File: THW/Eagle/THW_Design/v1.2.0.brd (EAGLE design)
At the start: 100 x 200 mm, 41 parts, among them U1 ADA4091-2ARZ-RL

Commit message: commit
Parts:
- removed C1: 0805YC103J4T2A, 0805YC103J4T2A:CAPC2012X94N
- removed R1, R2, R3: (no value), resistor:M0805
- removed U1: ADA4091-2ARZ-RL, ADA4091-2ARZ-RL:SOIC127P600X175-8N
- moved POWER 20.0 mm to (58.2, 199.9)
- moved TP3 20.0 mm to (40.1, 198.0)
- moved WB_SENS2 20.0 mm to (78.0, 199.9)
- moved TP1 19.8 mm to (54.1, 174.7)
- moved TP25 17.1 mm to (29.8, 163.8)
- moved R7 8.74 mm to (49.5, 173.4), turned to 180 degrees
- moved TP27 8.60 mm to (36.3, 166.7)
- moved R4 6.00 mm to (45.4, 173.4), turned to 180 degrees
- moved R_CURRENT 5.59 mm to (40.5, 174.7), turned to 270 degrees
- moved TP28 2.58 mm to (34.4, 163.8)
- moved TP26 1.42 mm to (31.7, 166.8)
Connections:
- removed net GND: C1.2, POWER.6, R3.2, U1.3, U1.4, WB_SENS2.8
- removed net LONG_HW+: U1.2
- removed net LONG_HW_SENS-: LONG_HW-.P$1, TP28.TP, WB_SENS1.2
- removed net N$2: R1.1, U1.5
- removed net N$4: R2.2, R3.1, U1.6
- removed net OPAMP_OUTPUT: R2.1, U1.7, WB_SENS2.7
- removed net SHORT_HW_SENS+: SHORT_HW+.P$2, TP26.TP, WB_SENS1.8
- removed net SHORT_HW_SENS-: LONG_HW+.P$2, SHORT_HW-.P$1, TP25.TP, TP27.TP, WB_SENS1.1, WB_SENS1.5, WB_SENS1.7
- removed net SUMMING_OP_AMP: R1.2, R4.1, R7.2, WB_SENS1.6, WB_SENS2.4, WB_SENS2.5
- removed net VSS: C1.1, POWER.5, U1.8
- new net NODE_B: R4.1, R7.2, WB_SENS1.7, WB_SENS2.4, WB_SENS2.6
- net SHORT_HW+: now also SHORT_HW+.P$2, TP26.TP, WB_SENS1.2, WB_SENS2.5, WB_SENS2.8; no longer WB_SENS2.2, WB_SENS2.3
- net SHORT_HW-: now also LONG_HW+.P$2, SHORT_HW-.P$1, TP25.TP, TP27.TP, WB_SENS1.1, WB_SENS1.6, WB_SENS1.8
- net WB_CURRENT+: now also POWER.2, WB_SENS2.7; no longer POWER.3, WB_SENS2.1
- net WB_CURRENT-: now also LONG_HW-.P$1, POWER.1, TP28.TP, WB_SENS1.5, WB_SENS2.3; no longer POWER.4, U1.1, WB_SENS2.6
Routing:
- net SHORT_HW-: track 14.8 -> 619.0 mm, vias 2 -> 7
- net SHORT_HW_SENS-: track 326.8 -> 0.00 mm, vias 2 -> 0
- net SHORT_HW+: track 59.5 -> 219.9 mm, vias 3 -> 5
- net WB_CURRENT-: track 65.3 -> 177.7 mm, vias 3 -> 4
- net NODE_B: track 0.00 -> 81.0 mm, vias 0 -> 3
- net PT_CURRENT-: track 212.6 -> 150.7 mm
- net WB_CURRENT+: track 28.5 -> 60.9 mm
- net PT_CURRENT+: track 330.4 -> 306.7 mm
- net PT3_S-: track 88.0 -> 82.6 mm
- net PT3_S+: track 84.5 -> 80.4 mm
- net SUMMING_OP_AMP: track 2.96 -> 0.00 mm, vias 2 -> 0
- net PT4_S+: track 213.8 -> 212.7 mm
- net PT0_S+: track 90.8 -> 89.8 mm
- net PT2_S-: track 132.3 -> 133.1 mm
- net PT2_S+: track 134.6 -> 134.0 mm
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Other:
- board text removed: "Wheatstone bridge"

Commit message: new traces
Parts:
- removed PT$0: PTS1206A, PTS1206:CAPMP3216X166
- removed R4, R7: (no value), resistor:M0805
- removed TP1, TP10, TP12, TP14, TP16, TP18, TP2, TP20, TP22, TP24, TP25, TP26, TP27, TP28, TP3, TP4, TP6, TP8: TPTP10SQ, testpad:TP10SQ
- added POT_1, POT_2, POT_LONG_HW, POT_SHORT_HW: 67WR200LFR$1, POTENTIOMETER_67WR200LFR:67WR200LF
- added PT$6: PTS1206A, PTS1206:CAPMP3216X166
- moved PT$1 89.4 mm to (50.0, 126.2), turned to 0 degrees
- moved PT$3 72.9 mm to (73.6, 61.1), flipped to the bottom, turned to 90 degrees
- moved PT$5 42.0 mm to (26.4, 40.1), turned to 90 degrees
- moved PT$2 42.0 mm to (73.6, 103.1), flipped to the top
- moved R_CURRENT 4.47 mm to (36.5, 172.7)
- moved PT$4 3.93 mm to (50.0, 16.8), turned to 180 degrees
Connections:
- removed net PT0_S+: PT$0.SENS+, PT_SENS2.3, TP2.TP
- removed net PT0_S-: PT$0.SENS-, PT_SENS2.4, TP4.TP
- removed net PT1_S+: PT$1.SENS+, PT_SENS1.2, TP10.TP
- removed net PT1_S-: PT$1.SENS-, PT_SENS1.1, TP12.TP
- removed net PT2_S+: PT$2.SENS+, PT_SENS2.5, TP6.TP
- removed net PT2_S-: PT$2.SENS-, PT_SENS2.6, TP8.TP
- removed net PT3_S+: PT$3.SENS+, PT_SENS2.2, TP18.TP
- removed net PT3_S-: PT$3.SENS-, PT_SENS2.1, TP20.TP
- removed net PT4_S+: PT$4.SENS+, PT_SENS2.8, TP14.TP
- removed net PT4_S-: PT$4.SENS-, PT_SENS2.7, TP16.TP
- removed net PT5_S+: PT$5.SENS+, PT_SENS1.4, TP22.TP
- removed net PT5_S-: PT$5.SENS-, PT_SENS1.3, TP24.TP
- new net N$1: LONG_HW-.P$1, LONG_HW-.P$2, POT_LONG_HW.P$2
- new net N$2: PT$1.-, PT$2.+, PT_SENS2.2, PT_SENS2.3
- new net N$3: PT$2.-, PT$3.+, PT_SENS2.4, PT_SENS2.5
- new net N$4: PT$3.-, PT$4.+, PT_SENS2.6, PT_SENS2.7
- new net N$5: PT$4.-, PT$5.+, PT_SENS1.1, PT_SENS2.8
- new net N$6: PT$5.-, PT$6.+, PT_SENS1.2, PT_SENS1.3
- new net N$8: POT_SHORT_HW.P$1, SHORT_HW+.P$1, SHORT_HW+.P$2
- net NODE_B: now also POT_1.P$1, POT_2.P$2, WB_SENS1.1; no longer R4.1, R7.2, WB_SENS1.7
- net PT_CURRENT+: now also PT_SENS2.1; no longer PT$0.+, PT$0.-, PT$1.-, PT$2.+, PT$2.-, PT$3.+, PT$3.-, PT$4.+, PT$4.-, PT$5.+, TP1.TP
- net PT_CURRENT-: now also PT$6.-, PT_SENS1.4; no longer PT$5.-, TP3.TP
- net SHORT_HW+: now also POT_1.P$2, POT_SHORT_HW.P$2; no longer R4.2, SHORT_HW+.P$1, SHORT_HW+.P$2, TP26.TP, WB_SENS1.2
- net SHORT_HW-: now also WB_SENS1.2; no longer TP25.TP, TP27.TP, WB_SENS1.1, WB_SENS1.6, WB_SENS1.8
- net WB_CURRENT-: now also POT_2.P$1, POT_LONG_HW.P$1, POWER.5; no longer LONG_HW-.P$1, LONG_HW-.P$2, POWER.1, R7.1, TP28.TP, WB_SENS1.5
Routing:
- net SHORT_HW-: track 619.0 -> 237.7 mm, vias 7 -> 4
- net PT_CURRENT+: track 306.7 -> 0.00 mm, vias 12 -> 0
- net PT4_S+: track 212.7 -> 0.00 mm, vias 2 -> 0
- net PT4_S-: track 206.2 -> 0.00 mm, vias 2 -> 0
- net SHORT_HW+: track 219.9 -> 20.7 mm, vias 5 -> 3
- net PT1_S+: track 159.7 -> 0.00 mm, vias 2 -> 0
- net PT1_S-: track 153.9 -> 0.00 mm, vias 2 -> 0
- net WB_CURRENT-: track 177.7 -> 25.9 mm, vias 4 -> 2
- net PT_CURRENT-: track 150.7 -> 0.00 mm, vias 2 -> 0
- net PT2_S+: track 134.0 -> 0.00 mm, vias 2 -> 0
- net PT2_S-: track 133.1 -> 0.00 mm, vias 2 -> 0
- net PT5_S+: track 114.2 -> 0.00 mm, vias 2 -> 0
- net PT5_S-: track 108.6 -> 0.00 mm, vias 2 -> 0
- net PT0_S+: track 89.8 -> 0.00 mm, vias 2 -> 0
- net PT0_S-: track 88.3 -> 0.00 mm, vias 2 -> 0
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
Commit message: Some polygon work for Asad
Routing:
- net WB_CURRENT-: track 25.9 -> 2.88 mm
- net SHORT_HW+: track 20.7 -> 2.02 mm
- net NODE_B: track 30.6 -> 22.1 mm
- net N$1: track 35.0 -> 28.7 mm
- net N$8: track 33.4 -> 29.3 mm
- added copper zone on layer 2, net N$1
- added copper zone on layer 2, net N$8
- added copper zone on layer 2, net NODE_B
- added copper zone on layer 2, net SHORT_HW+
- added copper zone on layer 2, net WB_CURRENT-
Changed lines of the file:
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@@
 <via x="52.21" y="170.34" extent="1-16" drill="0.35"/>
 <via x="46.88" y="172.8" extent="1-16" drill="0.35"/>
-<wire x1="50.81" y1="172.49" x2="49.4" y2="173.9" width="6.5" layer="2"/>
-<wire x1="49.4" y1="173.9" x2="49.30791875" y2="173.9" width="6.5" layer="2"/>
-<wire x1="49.4" y1="173.9" x2="44.9" y2="178.4" width="6.5" layer="2"/>
 <wire x1="29.4738" y1="178.4" x2="44.9" y2="178.4" width="6.5" layer="2"/>
 <contactref element="WB_SENS1" pad="1"/>
@@
 <wire x1="27.719" y1="182.588" x2="27.719" y2="180.1548" width="2" layer="2"/>
 <wire x1="27.719" y1="180.1548" x2="28.9869" y2="178.8869" width="2" layer="2"/>
+<polygon width="0.15" layer="2">
+<vertex x="53.9" y="169.4"/>
+<vertex x="49.1" y="169.4"/>
+<vertex x="43.5" y="175"/>
+<vertex x="43.5" y="181.4"/>
+<vertex x="43.6" y="181.5"/>
+<vertex x="48.4" y="181.5"/>
+<vertex x="49.2" y="180.7"/>
+<vertex x="49.2" y="178.4"/>
+<vertex x="53.9" y="173.7"/>
+</polygon>
 <wire x1="68.494" y1="184.65" x2="70.524" y2="184.65" width="0" layer="19" extent="1-1"/>
-<wire x1="50.81" y1="172.49" x2="68.494" y2="184.65" width="0" layer="19" extent="1-2"/>
-<wire x1="52.21" y1="170.34" x2="50.81" y2="172.49" width="0" layer="19" extent="1-2"/>
-<wire x1="46.88" y1="172.8" x2="49.30791875" y2="173.9" width="0" layer="19" extent="1-2"/>
+<wire x1="52.21" y1="170.34" x2="68.494" y2="184.65" width="0" layer="19" extent="1-1"/>
 </signal>
 <signal name="SHORT_HW+">
@@
 <contactref element="POT_SHORT_HW" pad="P$2"/>
 <contactref element="POT_1" pad="P$2"/>
-<via x="36.471" y="171.794" extent="1-16" drill="0.35"/>
 <via x="46.92" y="160.4" extent="1-16" drill="0.35"/>
-<wire x1="36.5" y1="168.2" x2="36.5" y2="169.1" width="6.5" layer="2"/>
-<wire x1="42.3476" y1="162.3524" x2="45.3" y2="162.3524" width="6.5" layer="2"/>
-<wire x1="36.5" y1="168.2" x2="42.3476" y2="162.3524" width="6.5" layer="2"/>
 <via x="46.88" y="170.3" extent="1-16" drill="0.35"/>
-<wire x1="36.5" y1="168.2" x2="37.4" y2="169.1" width="6.5" layer="2"/>
-<wire x1="37.4" y1="169.1" x2="44.7" y2="169.1" width="6.5" layer="2"/>
+<polygon width="0.1524" layer="2">
+<vertex x="35.5" y="172.5"/>
+<vertex x="45.5" y="172.5"/>
+<vertex x="48.4" y="169.6"/>
+<vertex x="48.4" y="159.2"/>
+<vertex x="35.5" y="159.2"/>
+</polygon>
+<wire x1="36.471" y1="171.794" x2="36.471" y2="169.8" width="1.27" layer="1"/>
+<wire x1="36.471" y1="169.8" x2="36.5" y2="169.8" width="0.1524" layer="1"/>
+<via x="36.5" y="169.8" extent="1-16" drill="0.35"/>
 <wire x1="72.554" y1="184.65" x2="71.544" y2="182.62" width="0" layer="19" extent="1-1"/>
 <wire x1="46.88" y1="170.3" x2="71.544" y2="182.62" width="0" layer="19" extent="1-1"/>
-<wire x1="44.7" y1="169.1" x2="46.88" y2="170.3" width="0" layer="19" extent="1-2"/>
-<wire x1="46.92" y1="160.4" x2="45.3" y2="162.3524" width="0" layer="19" extent="1-2"/>
-<wire x1="36.471" y1="171.794" x2="36.5" y2="169.1" width="0" layer="19" extent="1-2"/>
 </signal>
 <signal name="SHORT_HW-">
@@
 <via x="52.18" y="162.9" extent="1-16" drill="0.35"/>
 <via x="52.21" y="167.84" extent="1-16" drill="0.35"/>
-<wire x1="52.2" y1="165.45" x2="52.2" y2="164.92" width="6.5" layer="2"/>
-<wire x1="53.56551875" y1="165.8376" x2="57.4624" y2="169.73448125" width="6.5" layer="2"/>
-<wire x1="57.4624" y1="169.73448125" x2="57.4624" y2="175.24551875" width="6.5" layer="2"/>
-<wire x1="57.4624" y1="175.24551875" x2="54.553959375" y2="178.153959375" width="6.5" layer="2"/>
-<wire x1="52.2" y1="164.92" x2="53.1176" y2="165.8376" width="6.5" layer="2"/>
-<wire x1="53.1176" y1="165.8376" x2="53.56551875" y2="165.8376" width="6.5" layer="2"/>
-<wire x1="51.50551875" y1="179.6024" x2="52.953959375" y2="178.153959375" width="4" layer="2"/>
 <contactref element="POWER" pad="5"/>
-<wire x1="54.553959375" y1="178.153959375" x2="52.953959375" y2="178.153959375" width="4" layer="2"/>
-<wire x1="51.753" y1="179.35491875" x2="52.953959375" y2="178.153959375" width="1.27" layer="2"/>
 <wire x1="51.753" y1="182.665" x2="51.753" y2="179.84988125" width="2" layer="2"/>
-<wire x1="51.753" y1="179.84988125" x2="51.50551875" y2="179.6024" width="2" layer="2"/>
-<wire x1="57.4624" y1="175.24551875" x2="69.514" y2="182.62" width="0" layer="19" extent="1-2"/>
-<wire x1="52.18" y1="162.9" x2="52.2" y2="164.92" width="0" layer="19" extent="1-2"/>
-<wire x1="52.21" y1="167.84" x2="53.1176" y2="165.8376" width="0" layer="19" extent="1-2"/>
+<wire x1="57.4624" y1="168.7" x2="57.4" y2="168.7" width="0.1524" layer="2"/>
+<polygon width="0.15" layer="2">
+<vertex x="49" y="161.8"/>
+<vertex x="49" y="169"/>
+<vertex x="54.4" y="169"/>
+<vertex x="54.4" y="173.8"/>
+<vertex x="49.6" y="178.6"/>
+<vertex x="49.6" y="181.4"/>
+<vertex x="61.1" y="181.4"/>
+<vertex x="61.1" y="161.8"/>
+</polygon>
+<wire x1="51.753" y1="182.665" x2="69.514" y2="182.62" width="0" layer="19" extent="1-1"/>
 </signal>
 <signal name="PT_CURRENT-">
@@
 <wire x1="56.479" y1="122.458" x2="56.48" y2="122.459" width="0.2" layer="2" curve="-90"/>
 <via x="52.18" y="160.4" extent="1-16" drill="0.35"/>
-<wire x1="57" y1="153.3" x2="52.6" y2="157.7" width="6.5" layer="2"/>
 <wire x1="57" y1="124.559" x2="57" y2="153.3" width="6.5" layer="2"/>
-<wire x1="52.6" y1="157.7" x2="52.18" y2="160.4" width="0" layer="19" extent="1-2"/>
-<wire x1="57.556" y1="122.459" x2="57" y2="124.559" width="0" layer="19" extent="1-2"/>
+<polygon width="0.1524" layer="2">
+<vertex x="49" y="161.4"/>
+<vertex x="61.1" y="161.4"/>
+<vertex x="61.1" y="152"/>
+<vertex x="49" y="152"/>
+</polygon>
 <wire x1="56.479" y1="122.458" x2="57.556" y2="122.459" width="0" layer="19" extent="1-1"/>
+<wire x1="57" y1="124.559" x2="57.556" y2="122.459" width="0" layer="19" extent="1-2"/>
 </signal>
 <signal name="N$8">
@@
 <via x="42.479" y="122.438" extent="1-16" drill="0.35"/>
 <via x="43.556" y="122.439" extent="1-16" drill="0.35"/>
-<wire x1="43" y1="124.539" x2="43" y2="139.5" width="6.5" layer="2"/>
-<wire x1="43" y1="139.5" x2="43" y2="143.3" width="6.5" layer="2"/>
-<wire x1="43" y1="143.3" x2="43" y2="143.3" width="6.5" layer="2"/>
+<wire x1="43" y1="124.539" x2="43" y2="143.3" width="6.5" layer="2"/>
 <wire x1="43" y1="143.3" x2="43" y2="152.8" width="6.5" layer="2"/>
-<wire x1="45.9" y1="155.7" x2="43" y2="152.8" width="6.5" layer="2"/>
 <wire x1="43.556" y1="122.439" x2="42.48" y2="122.439" width="0.4064" layer="2"/>
 <wire x1="42.48" y1="122.439" x2="42.479" y2="122.438" width="0.4064" layer="2"/>
 <via x="46.92" y="157.9" extent="1-16" drill="0.35"/>
-<wire x1="45.9" y1="155.7" x2="46.92" y2="157.9" width="0" layer="19" extent="1-2"/>
-<wire x1="43.556" y1="122.439" x2="43" y2="124.539" width="0" layer="19" extent="1-2"/>
+<polygon width="0.1524" layer="2">
+<vertex x="48.5" y="158.8"/>
+<vertex x="39.7" y="158.8"/>
+<vertex x="39.7" y="152.3"/>
+<vertex x="48.4" y="152.3"/>
+<vertex x="48.5" y="152.3"/>
+</polygon>
+<wire x1="43" y1="124.539" x2="43.556" y2="122.439" width="0" layer="19" extent="1-2"/>
 </signal>
 </signals>

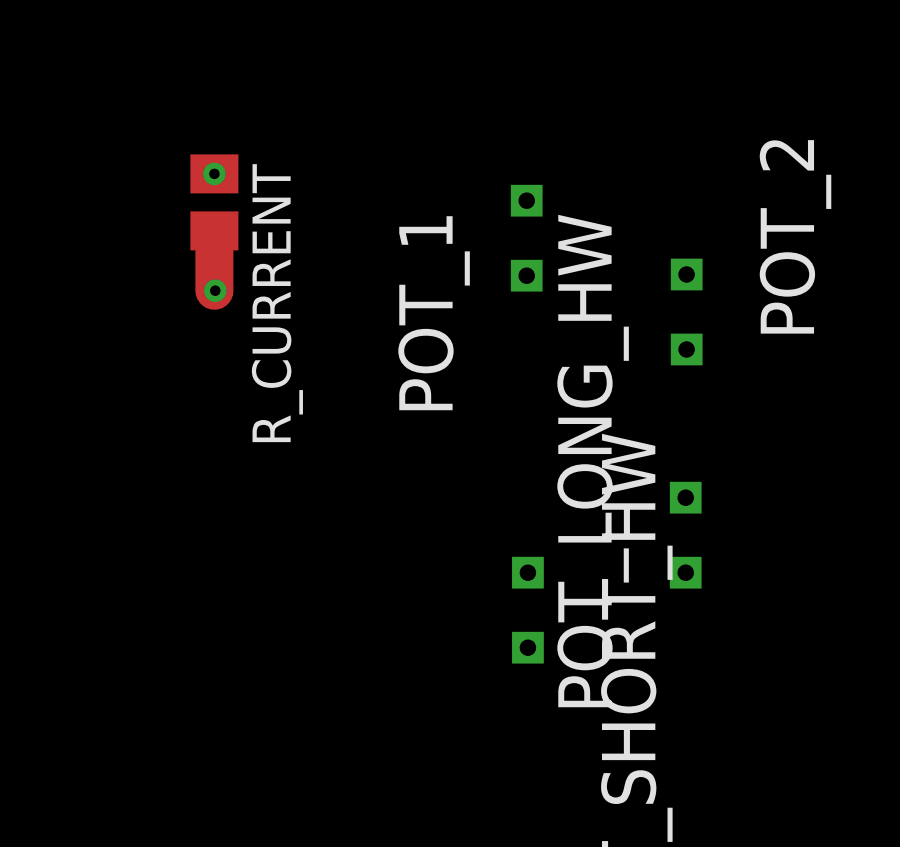
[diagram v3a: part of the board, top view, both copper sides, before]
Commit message: finish routing pt sensors tomorrow
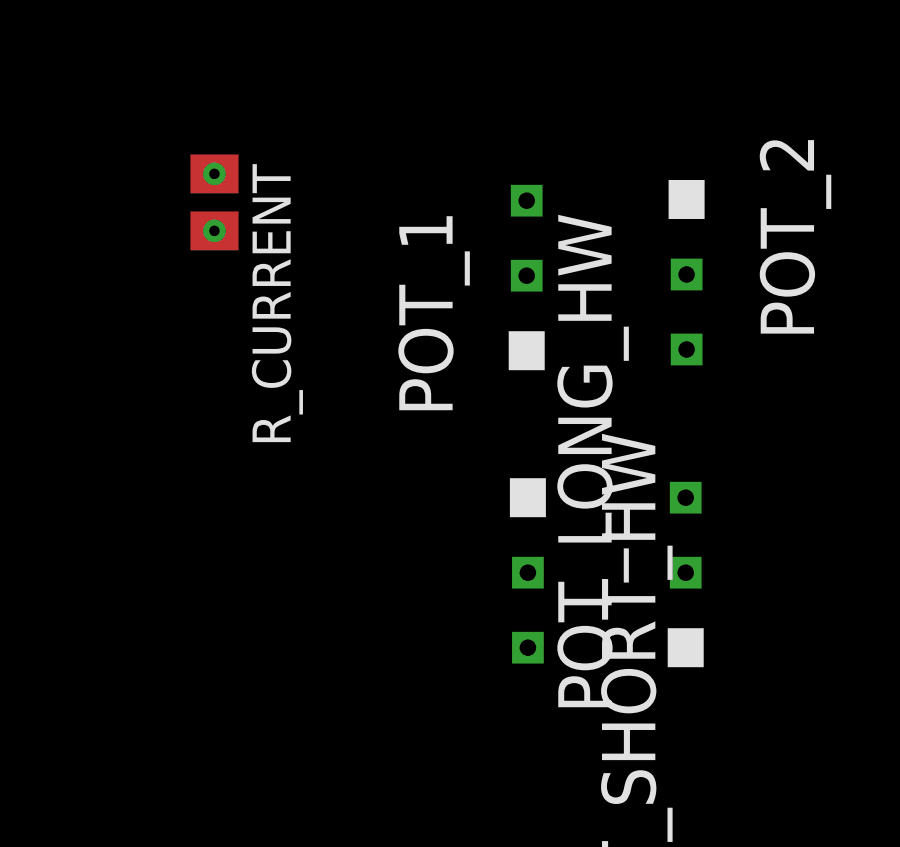
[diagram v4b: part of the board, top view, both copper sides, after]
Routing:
- net N$7: track 29.3 -> 0.00 mm, vias 3 -> 2
- net N$1: track 28.7 -> 0.00 mm, vias 3 -> 2
- net SHORT_HW-: track 237.7 -> 211.6 mm
- net NODE_B: track 22.1 -> 2.43 mm, vias 2 -> 0
- net WB_CURRENT+: track 15.5 -> 1.93 mm
- net N$8: track 0.00 -> 9.50 mm
- net SHORT_HW+: track 2.02 -> 1.83 mm, vias 3 -> 1
- net WB_CURRENT-: vias 2 -> 0
- added copper zone on layer 2, net N$8
- added copper zone on layer 2, net SHORT_HW-
- added copper zone on layer 3, net WB_CURRENT+
- removed copper zone on layer 2, net N$7

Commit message: added the cool logo
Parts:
- turned PT$2 to 90 degrees
- turned PT$5 to 270 degrees
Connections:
- net N$1: now also WB_SENS2.8
- net N$5: now also PT_SENS1.2; no longer PT_SENS1.1
- net N$6: now also PT_SENS1.1, PT_SENS1.7; no longer PT_SENS1.2, PT_SENS1.3
- net N$7: now also WB_SENS2.6
- net NODE_B: now also WB_SENS2.2; no longer WB_SENS2.6
- net PT_CURRENT-: now also PT_SENS1.8; no longer PT_SENS1.4
- net SHORT_HW+: now also WB_SENS1.4, WB_SENS2.3; no longer WB_SENS2.8
- net WB_CURRENT+: now also WB_SENS1.3; no longer WB_SENS2.7
- net WB_CURRENT-: now also POWER.1, WB_SENS2.1, WB_SENS2.7; no longer POWER.5, WB_SENS2.3
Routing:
- net N$5: track 0.00 -> 419.1 mm, vias 0 -> 3
- net N$4: track 0.00 -> 407.5 mm, vias 0 -> 3
- net N$6: track 0.00 -> 306.4 mm, vias 0 -> 2
- net N$3: track 0.00 -> 264.4 mm, vias 0 -> 2
- net PT_CURRENT-: track 0.00 -> 252.6 mm, vias 0 -> 3
- net N$2: track 0.00 -> 222.1 mm, vias 0 -> 3
- net PT_CURRENT+: track 0.00 -> 156.7 mm, vias 0 -> 2
- net SHORT_HW+: track 1.83 -> 90.0 mm
- net N$7: track 0.00 -> 57.9 mm
- net WB_CURRENT-: track 2.88 -> 59.8 mm
- net NODE_B: track 2.43 -> 51.5 mm
- net N$1: track 0.00 -> 40.1 mm
- net WB_CURRENT+: track 1.93 -> 13.6 mm
- net SHORT_HW-: track 211.6 -> 207.0 mm

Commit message: stitching
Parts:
- moved LONG_HW- 25.0 mm to (57.0, 97.4)
- moved LONG_HW+ 25.0 mm to (57.0, 45.7)
- turned PT$1 to 180 degrees
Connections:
- removed net N$2: PT$1.-, PT$2.+, PT_SENS2.2, PT_SENS2.3
- new net N$9: PT$1.-, PT$2.+, PT_SENS2.1, PT_SENS2.3
- net PT_CURRENT+: now also PT_SENS2.2; no longer PT_SENS2.1
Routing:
- net N$2: track 222.1 -> 0.00 mm, vias 3 -> 1
- net N$9: track 0.00 -> 206.5 mm, vias 0 -> 3
- net N$5: track 419.1 -> 409.3 mm
- net N$8: track 9.50 -> 0.00 mm, vias 0 -> 1
- net N$7: track 57.9 -> 67.4 mm, vias 2 -> 3
- net N$6: track 306.4 -> 298.4 mm
- net N$4: track 407.5 -> 404.3 mm
- net PT_CURRENT+: track 156.7 -> 159.5 mm
- net SHORT_HW+: track 90.0 -> 91.2 mm
- net N$3: track 264.4 -> 265.5 mm
- net PT_CURRENT-: track 252.6 -> 253.7 mm
- net SHORT_HW-: vias 4 -> 6
- net N$1: vias 2 -> 3
- added copper zone on layer 2, net N$7
- removed copper zone on layer 2, net N$8
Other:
- outline, holes or cut-outs redrawn
